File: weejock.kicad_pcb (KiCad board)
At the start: 2 copper layers, 95.4 x 89.7 mm, 44 parts, among them J2 JST-PH2, K1 PG1350, K10 PG1350, K11 PG1350, K12 PG1350, K13 PG1350, K14 PG1350, K15 PG1350, K16 PG1350, K17 PG1350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

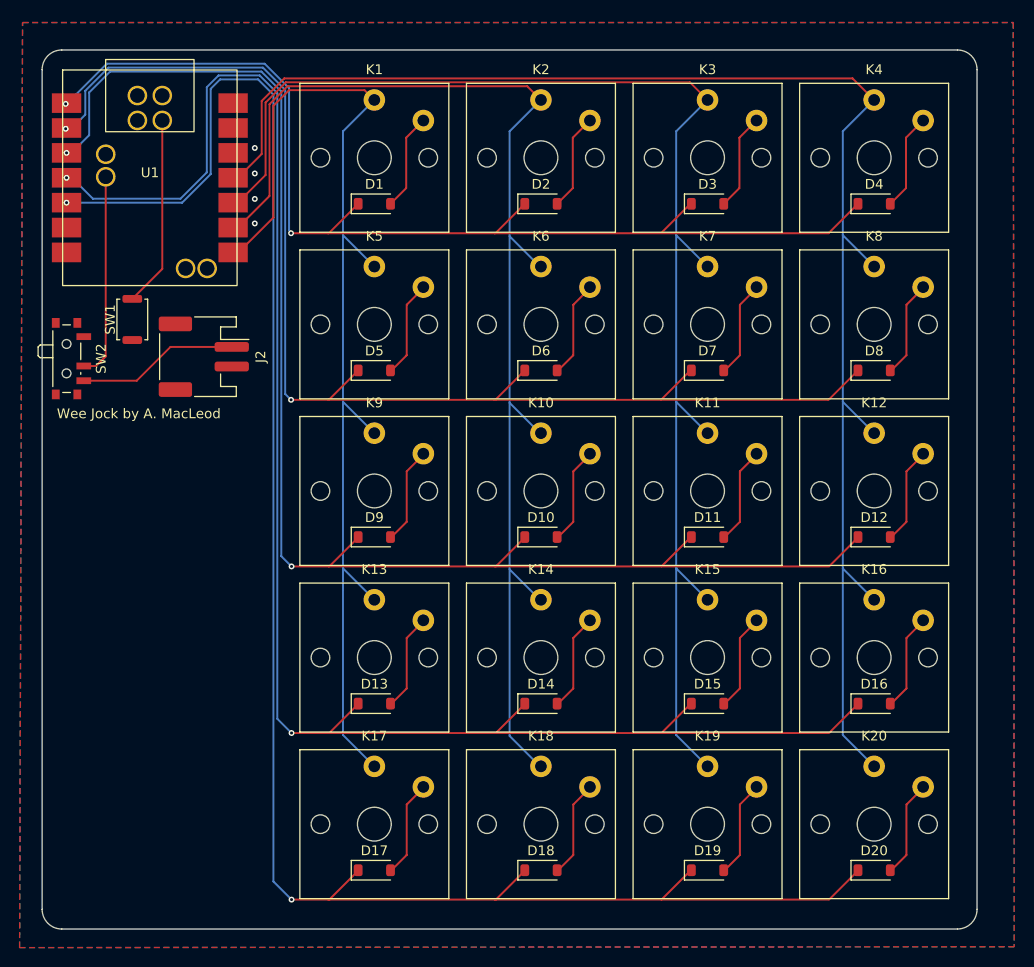
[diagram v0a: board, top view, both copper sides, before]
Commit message: Version 0.0.2 - use footprint that is both SMT and through hole friendly, and fix JST footprint.
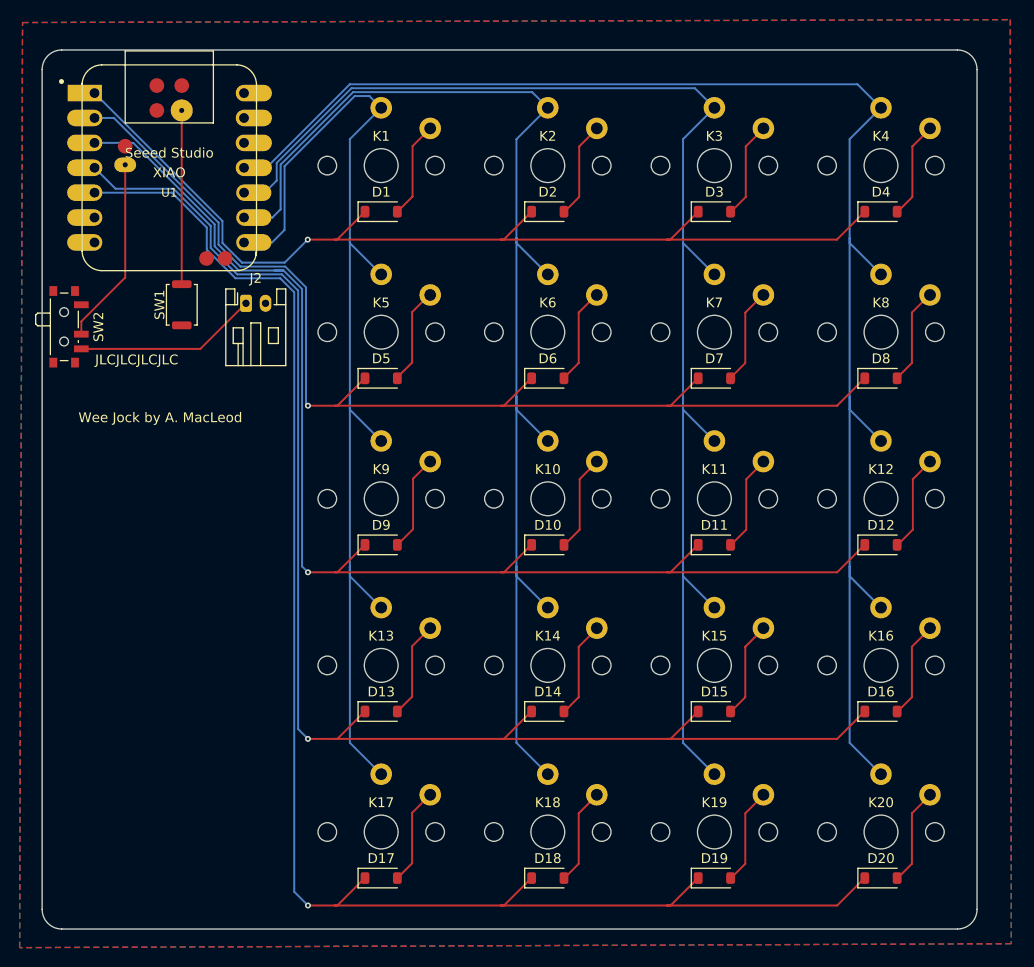
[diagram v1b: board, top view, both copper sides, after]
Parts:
- J2: footprint Connector_JST:JST_PH_S2B-PH-SM4-TB_1x02-1MP_P2.00mm_Horizontal -> Connector_JST:JST_PH_S2B-PH-K_1x02_P2.00mm_Horizontal
- K1, K10, K11, K12, K13, K14, K15, K16, K17, K18, K19, K2, K20, K3, K4, K5, K6, K7, K8, K9: footprint Switch_Keyboard_Kailh:SW_Kailh_Choc_V1 -> weejock_library:SW_Kailh_Choc_V1
- U1: footprint weejock_library:Seeed XIAO Simplified -> weejock_library:Castellated XIAO with BAT+ and RST
- moved J2 6.94 mm to (95.4, 73.2), turned to 0 degrees
- moved SW1 5.27 mm to (88.8, 73.3)
- moved SW2 3.26 mm to (77.2, 75.5)
- moved U1 2.21 mm to (87.6, 59.3)
- moved D17 1.06 mm to (109.2, 131.8)
- moved D18 1.06 mm to (126.2, 131.8)
- moved K1 1.06 mm to (109.2, 59.1)
- moved K2 1.06 mm to (126.2, 59.1)
- moved D19 1.06 mm to (143.2, 131.8)
- moved D20 1.06 mm to (160.2, 131.8)
- moved D1 1.06 mm to (109.2, 63.8)
- moved D10 1.06 mm to (126.2, 97.8)
- moved D13 1.06 mm to (109.2, 114.8)
- moved D14 1.06 mm to (126.2, 114.8)
- moved D2 1.06 mm to (126.2, 63.8)
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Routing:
- net row3: track 171.6 -> 144.5 mm, vias 2 -> 1
- net row4: track 186.7 -> 160.1 mm, vias 2 -> 1
- net row2: track 149.4 -> 129.8 mm, vias 2 -> 1
- net row1: track 131.0 -> 113.2 mm, vias 2 -> 1
- net row0: track 112.4 -> 102.2 mm, vias 2 -> 1
- net col0: track 115.6 -> 111.5 mm
- net BAT+: track 22.0 -> 19.1 mm
- net Net-(J2-Pin_1): track 16.5 -> 18.7 mm
- net RST: track 19.5 -> 17.7 mm
- net col2: track 143.0 -> 141.3 mm
- net col3: track 158.0 -> 156.6 mm
- net col1: track 127.9 -> 126.7 mm
- net GND: track 0.50 -> 0.00 mm, vias 4 -> 0
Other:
- board text added: "JLCJLCJLCJLC"

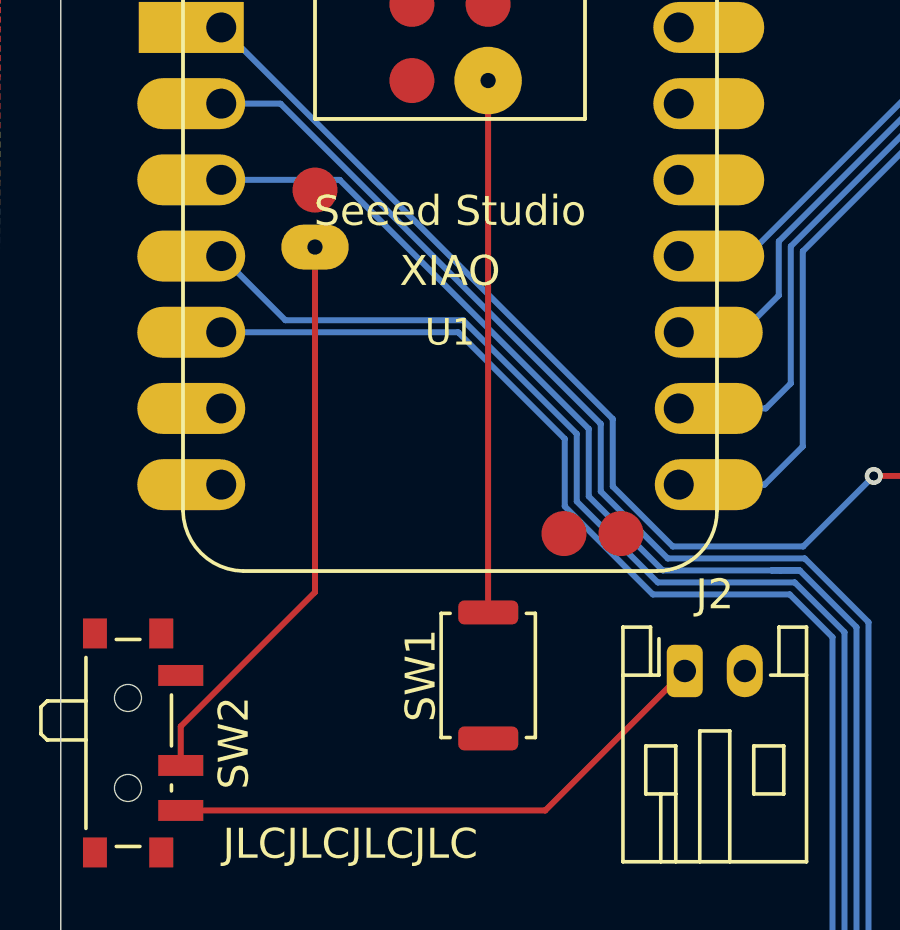
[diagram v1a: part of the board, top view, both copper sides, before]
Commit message: Minor changes, I think due to moving some text.
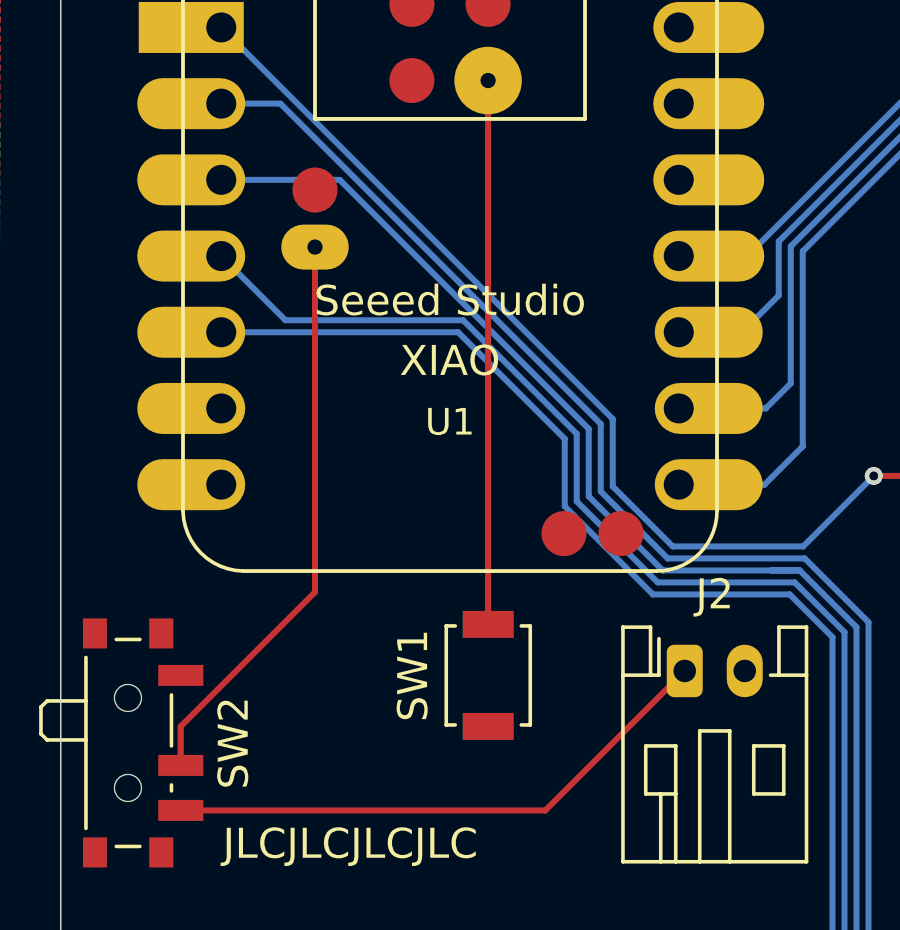
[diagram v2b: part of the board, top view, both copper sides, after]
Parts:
- SW1: footprint Button_Switch_SMD:SW_Push_SPST_NO_Alps_SKRK -> Button_Switch_SMD:SW_SPST_B3U-1000P
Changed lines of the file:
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@@
 			)
 		)
+		(property ki_fp_filters "Choc_v1")
 		(sheetname "Root")
 		(sheetfile "weejock.kicad_sch")
@@
 			)
 		)
+		(property ki_fp_filters "Choc_v1")
 		(sheetname "Root")
 		(sheetfile "weejock.kicad_sch")
@@
 			)
 		)
+		(property ki_fp_filters "Choc_v1")
 		(sheetname "Root")
 		(sheetfile "weejock.kicad_sch")
@@
 		(at 87.575 59.32)
 		(property "Reference" "U1"
-			(at 0 2.54 0)
+			(at 0 5.54 0)
 			(layer "F.SilkS")
 			(effects
@@
 		(fp_arc
 			(start 6.9 -10.5)
-			(mid 8.301494 -9.901494)
+			(mid 8.301492 -9.901492)
 			(end 8.9 -8.5)
 			(stroke
@@
 			(layer "F.Fab")
 		)
-		(fp_text user "Seeed Studio"
-			(at 0 -1.5 0)
+		(fp_text user "XIAO"
+			(at 0 3.5 0)
 			(unlocked yes)
 			(layer "F.SilkS")
@@
 			)
 		)
-		(fp_text user "XIAO"
-			(at 0 0.5 0)
+		(fp_text user "Seeed Studio"
+			(at 0 1.5 0)
 			(unlocked yes)
 			(layer "F.SilkS")
@@
 			)
 		)
+		(property ki_fp_filters "Choc_v1")
 		(sheetname "Root")
 		(sheetfile "weejock.kicad_sch")
@@
 			)
 		)
+		(property ki_fp_filters "Choc_v1")
 		(sheetname "Root")
 		(sheetfile "weejock.kicad_sch")
@@
 			)
 		)
+		(property ki_fp_filters "Choc_v1")
 		(sheetname "Root")
 		(sheetfile "weejock.kicad_sch")
@@
 			)
 		)
+		(property ki_fp_filters "Choc_v1")
 		(sheetname "Root")
 		(sheetfile "weejock.kicad_sch")
@@
 			)
 		)
+		(property ki_fp_filters "Choc_v1")
 		(sheetname "Root")
 		(sheetfile "weejock.kicad_sch")
@@
 			)
 		)
+		(property ki_fp_filters "Choc_v1")
 		(sheetname "Root")
 		(sheetfile "weejock.kicad_sch")
@@
 			)
 		)
+		(property ki_fp_filters "Choc_v1")
 		(sheetname "Root")
 		(sheetfile "weejock.kicad_sch")
@@
 			)
 		)
+		(property ki_fp_filters "Choc_v1")
 		(sheetname "Root")
 		(sheetfile "weejock.kicad_sch")
@@
 		)
 	)
-	(footprint "Button_Switch_SMD:SW_Push_SPST_NO_Alps_SKRK"
+	(footprint "Button_Switch_SMD:SW_SPST_B3U-1000P"
 		(layer "F.Cu")
 		(at 88.85 73.3 90)
-		(descr "http://www.alps.com/prod/info/E/HTML/Tact/SurfaceMount/SKRK/SKRKAHE020.html")
-		(tags "SMD SMT button")
+		(descr "Ultra-small-sized Tactile Switch with High Contact Reliability, Top-actuated Model, without Ground Terminal, without Boss")
+		(tags "Tactile Switch")
 		(property "Reference" "SW1"
-			(at 0 -2.25 90)
+			(at 0 -2.5 90)
 			(layer "F.SilkS")
 			(effects
@@
 			)
 		)
-		(property "Footprint" "Button_Switch_SMD:SW_Push_SPST_NO_Alps_SKRK"
+		(property "Footprint" "Button_Switch_SMD:SW_SPST_B3U-1000P"
 			(at 0 0 90)
 			(unlocked yes)
@@
 		(attr smd)
 		(fp_line
-			(start 2.07 -1.57)
-			(end 2.07 -1.27)
+			(start 1.65 -1.4)
+			(end 1.65 -1.1)
 			(stroke
 				(width 0.12)
@@
 		)
 		(fp_line
-			(start -2.07 -1.57)
-			(end 2.07 -1.57)
+			(start -1.65 -1.4)
+			(end 1.65 -1.4)
 			(stroke
 				(width 0.12)
@@
 		)
 		(fp_line
-			(start -2.07 -1.27)
-			(end -2.07 -1.57)
+			(start -1.65 -1.1)
+			(end -1.65 -1.4)
 			(stroke
 				(width 0.12)
@@
 		)
 		(fp_line
-			(start 2.07 1.27)
-			(end 2.07 1.57)
+			(start -1.65 1.1)
+			(end -1.65 1.4)
 			(stroke
 				(width 0.12)
@@
 		)
 		(fp_line
-			(start 2.07 1.57)
-			(end -2.07 1.57)
+			(start 1.65 1.4)
+			(end 1.65 1.1)
 			(stroke
 				(width 0.12)
@@
 		)
 		(fp_line
-			(start -2.07 1.57)
-			(end -2.07 1.27)
+			(start -1.65 1.4)
+			(end 1.65 1.4)
 			(stroke
 				(width 0.12)
@@
 		)
 		(fp_line
-			(start 2.75 -1.7)
-			(end 2.75 1.7)
+			(start 2.4 -1.65)
+			(end -2.4 -1.65)
 			(stroke
 				(width 0.05)
@@
 		)
 		(fp_line
-			(start -2.75 -1.7)
-			(end 2.75 -1.7)
+			(start -2.4 -1.65)
+			(end -2.4 1.65)
 			(stroke
 				(width 0.05)
@@
 		)
 		(fp_line
-			(start 2.75 1.7)
-			(end -2.75 1.7)
+			(start 2.4 1.65)
+			(end 2.4 -1.65)
 			(stroke
 				(width 0.05)
@@
 		)
 		(fp_line
-			(start -2.75 1.7)
-			(end -2.75 -1.7)
+			(start -2.4 1.65)
+			(end 2.4 1.65)
 			(stroke
 				(width 0.05)
@@
 		)
 		(fp_line
-			(start 1.95 -1.45)
-			(end 1.95 1.45)
+			(start 1.5 -1.25)
+			(end 1.5 1.25)
 			(stroke
 				(width 0.1)
@@
 		)
 		(fp_line
-			(start -1.95 -1.45)
-			(end 1.95 -1.45)
+			(start -1.5 -1.25)
+			(end 1.5 -1.25)
 			(stroke
 				(width 0.1)
@@
 		)
 		(fp_line
-			(start 1.95 1.45)
-			(end -1.95 1.45)
+			(start 1.5 1.25)
+			(end -1.5 1.25)
 			(stroke
 				(width 0.1)
@@
 		)
 		(fp_line
-			(start -1.95 1.45)
-			(end -1.95 -1.45)
+			(start -1.5 1.25)
+			(end -1.5 -1.25)
 			(stroke
 				(width 0.1)
@@
 		(fp_circle
 			(center 0 0)
-			(end 1 0)
+			(end 0.75 0)
 			(stroke
 				(width 0.1)
@@
 		)
 		(fp_text user "${REFERENCE}"
-			(at 0 0 90)
+			(at 0 -2.5 90)
 			(layer "F.Fab")
 			(effects
@@
 			)
 		)
-		(pad "1" smd roundrect
-			(at -2.1 0 90)
-			(size 0.8 2)
+		(pad "1" smd rect
+			(at -1.7 0 90)
+			(size 0.9 1.7)
 			(layers "F.Cu" "F.Paste" "F.Mask")
-			(roundrect_rratio 0.25)
 			(net 26 "GND")
 			(pinfunction "1")
 			(pintype "passive")
 		)
-		(pad "2" smd roundrect
-			(at 2.1 0 90)
-			(size 0.8 2)
+		(pad "2" smd rect
+			(at 1.7 0 90)
+			(size 0.9 1.7)
 			(layers "F.Cu" "F.Paste" "F.Mask")
-			(roundrect_rratio 0.25)
 			(net 32 "RST")
 			(pinfunction "2")
 			(pintype "passive")
 		)
-		(model "${KICAD8_3DMODEL_DIR}/Button_Switch_SMD.3dshapes/SW_Push_SPST_NO_Alps_SKRK.wrl"
+		(model "${KICAD8_3DMODEL_DIR}/Button_Switch_SMD.3dshapes/SW_SPST_B3U-1000P.wrl"
 			(offset
 				(xyz 0 0 0)
@@
 			)
 		)
+		(property ki_fp_filters "Choc_v1")
 		(sheetname "Root")
 		(sheetfile "weejock.kicad_sch")
@@
 			)
 		)
+		(property ki_fp_filters "Choc_v1")
 		(sheetname "Root")
 		(sheetfile "weejock.kicad_sch")
@@
 			)
 		)
+		(property ki_fp_filters "Choc_v1")
 		(sheetname "Root")
 		(sheetfile "weejock.kicad_sch")
@@
 			)
 		)
+		(property ki_fp_filters "Choc_v1")
 		(sheetname "Root")
 		(sheetfile "weejock.kicad_sch")
@@
 			)
 		)
+		(property ki_fp_filters "Choc_v1")
 		(sheetname "Root")
 		(sheetfile "weejock.kicad_sch")
@@
 			)
 		)
+		(property ki_fp_filters "Choc_v1")
 		(sheetname "Root")
 		(sheetfile "weejock.kicad_sch")
@@
 			)
 		)
+		(property ki_fp_filters "Choc_v1")
 		(sheetname "Root")
 		(sheetfile "weejock.kicad_sch")
@@
 			)
 		)
+		(property ki_fp_filters "Choc_v1")
 		(sheetname "Root")
 		(sheetfile "weejock.kicad_sch")
@@
 			)
 		)
+		(property ki_fp_filters "Choc_v1")
 		(sheetname "Root")
 		(sheetfile "weejock.kicad_sch")

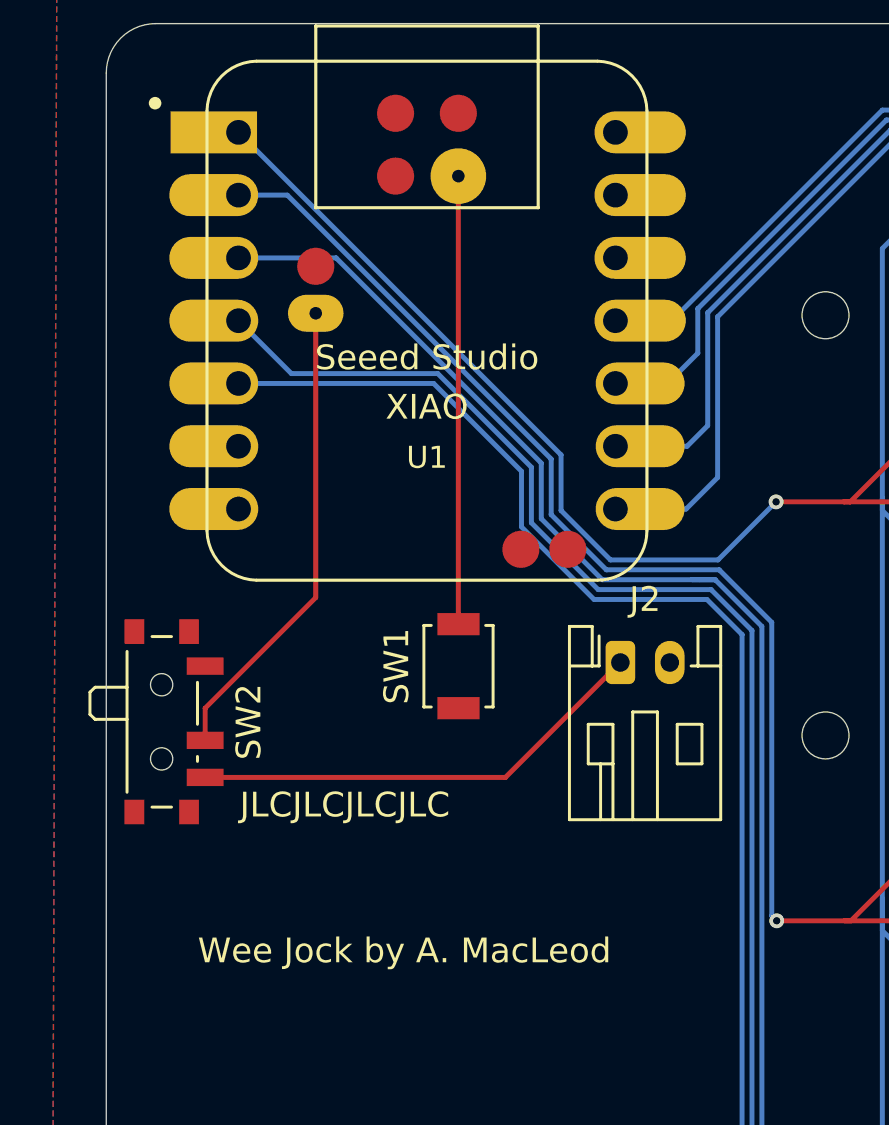
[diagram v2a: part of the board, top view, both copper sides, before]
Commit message: Rev 3: Fix up pad placement and silkscreen labels, as well as repositioning components a little. (#5)
* Correcting XIAO BLE footprint to reverse accidental mirroring of pads.

* Neatening power switch and adding ON/OFF labels.

* Labeling reset button.

* Moving JST jack for better keycap clearance, and adding +/- labels.

* Messing with labels.

* Update sheet metadata to reflect version number 0.0.3
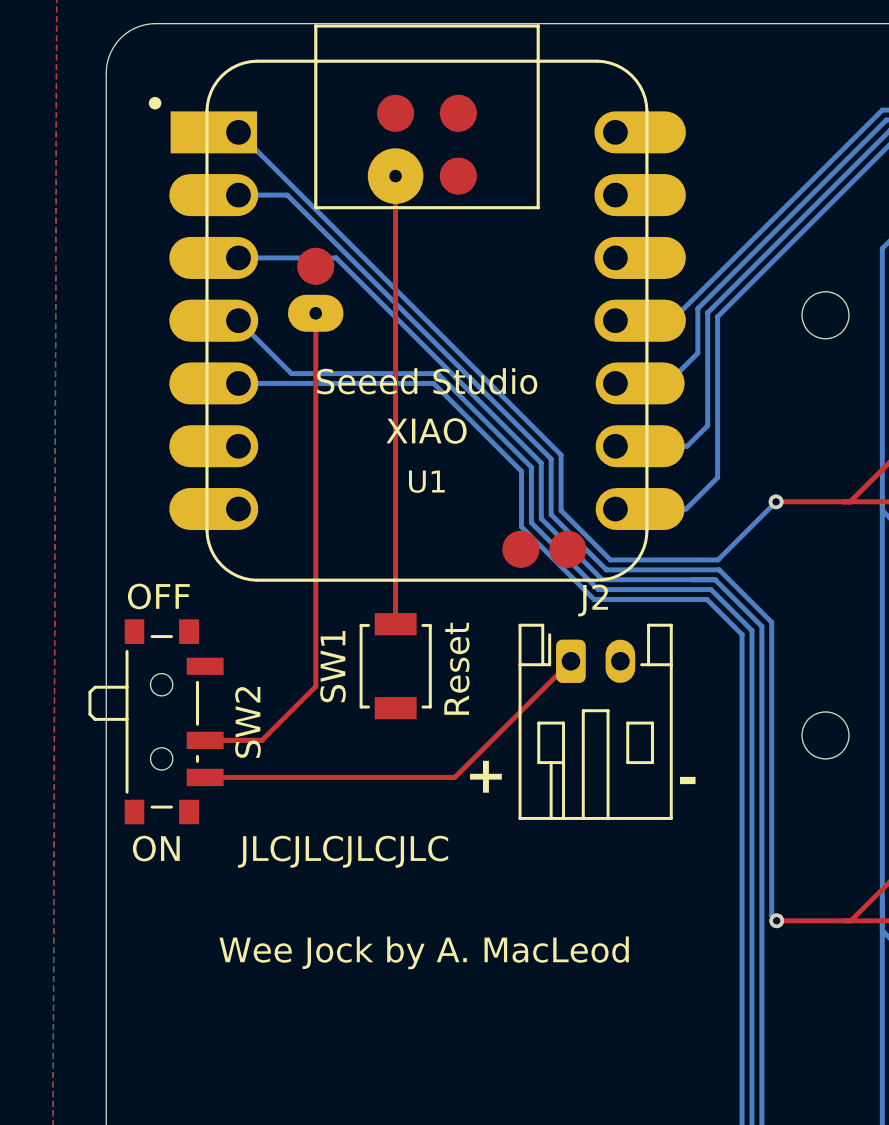
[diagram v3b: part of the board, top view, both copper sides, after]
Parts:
- moved SW1 2.54 mm to (86.3, 73.3)
- moved J2 2.00 mm to (93.4, 73.1)
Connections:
- net Net-(J2-Pin_1) renamed /B+ Supply
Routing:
- net /B+ Supply: track 18.7 -> 16.7 mm
- net BAT+: track 19.1 -> 20.5 mm
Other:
- board text added: "(rev. 3)"
- board text added: "+"
- board text added: "-"
- board text added: "OFF"
- board text added: "ON"
- board text added: "Reset"
